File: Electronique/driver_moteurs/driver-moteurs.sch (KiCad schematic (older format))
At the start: 19 parts, among them P1 CONN_01X12, P2 CONN_01X02, P3 CONN_I2C, P4 CONN_01X04, P5 CONN_01X03, P6 CONN_SERIAL, P7 CONN_SWDIO, P8 CONN_CAN, U1 stm32f303k8t6, U2 MCP2562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

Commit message: modif moteur axe z
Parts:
- removed P1: CONN_01X12, symbol CONN_01X12
- removed P2: CONN_01X02, symbol CONN_01X02
- removed P4: CONN_01X04, symbol CONN_01X04
- removed P5: CONN_01X03, symbol CONN_01X03
- added P1: CONN_ENCODER, symbol CONN_01X04
- added P2: CONN_FREE_3, symbol CONN_01X03
- added P4: CONN_01X03, symbol CONN_01X03
- added R11: 10kR, symbol R
- added U6: MC33926, symbol MC33926
- added U7: 74HC04, symbol 74HC04
- added U8: 74LS126, symbol 74LS126
- R2: value R -> 470R
- U1: footprint (none) -> Housings_QFP:LQFP-32_7x7mm_Pitch0.8mm
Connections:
- net labels added: +9V, EN_Servo, RX_Servo, TX_Servo, TX_servo
- wire segments 94 -> 124
- no-connect marks 4 -> 0
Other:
- moved on the sheet: D1, P6, R2

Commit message: axe z routage en cours
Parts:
- removed P2: CONN_FREE_3, symbol CONN_01X03
- added P2: CONN_02_FREE, Connectors_Molex:Molex_KK-6410-02_02x2.54mm_Straight, symbol CONN_01X02
- added P5: CONN_FC, Connectors_Molex:Molex_KK-6410-02_02x2.54mm_Straight, symbol CONN_01X02
- added U10, U11, U12, U13: Trou-3, axe_z:Trou-3, symbol Trou-3
- C1, C2, C3: footprint (none) -> Capacitors_SMD:C_1206_HandSoldering
- D1: footprint (none) -> Diodes_SMD:D_SMA-SMB_Universal_Handsoldering
- JP1: footprint (none) -> Pin_Headers:Pin_Header_Straight_1x03_Pitch2.54mm
- P1, P7: footprint (none) -> Connectors_Molex:Molex_KK-6410-04_04x2.54mm_Straight
- P3, P6, P8: footprint (none) -> Connectors_Molex:Molex_KK-6410-02_02x2.54mm_Straight
- P4: value CONN_01X03 -> CONN_Servo; footprint (none) -> Connectors_Molex:Molex_KK-6410-03_03x2.54mm_Straight
- R1, R11, R2, R3: footprint (none) -> Resistors_SMD:R_1206_HandSoldering
- U2: footprint (none) -> Housings_SOIC:SOIC-8_3.9x4.9mm_Pitch1.27mm
- U6: footprint (none) -> axe_z:MC33926
- U7, U8: footprint (none) -> Housings_DIP:DIP-14_W7.62mm_Socket
- Y1: footprint (none) -> Crystals:Crystal_HC18-U_Vertical
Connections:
- net +3V3: now also P5.2 (P2)
- net GND: now also U10.1 (GND), U11.1 (GND), U12.1 (GND), U13.1 (GND)
- net at U1.26 (PB3): now also P5.1 (P1)
- net at U1.27 (PB4): now also P2.2 (P2)
- net at U1.28 (PB5): now also P2.1 (P1)

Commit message: Correction schéma driver
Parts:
- D1: symbol LED -> LED-RESCUE-driver-moteurs
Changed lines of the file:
@@
 EESchema Schematic File Version 2
+LIBS:driver-moteurs-rescue
 LIBS:power
 LIBS:device
@@
 $EndComp
 $Comp
-L LED D1
+L LED-RESCUE-driver-moteurs D1
 U 1 1 59F77A31
 P 5700 1600

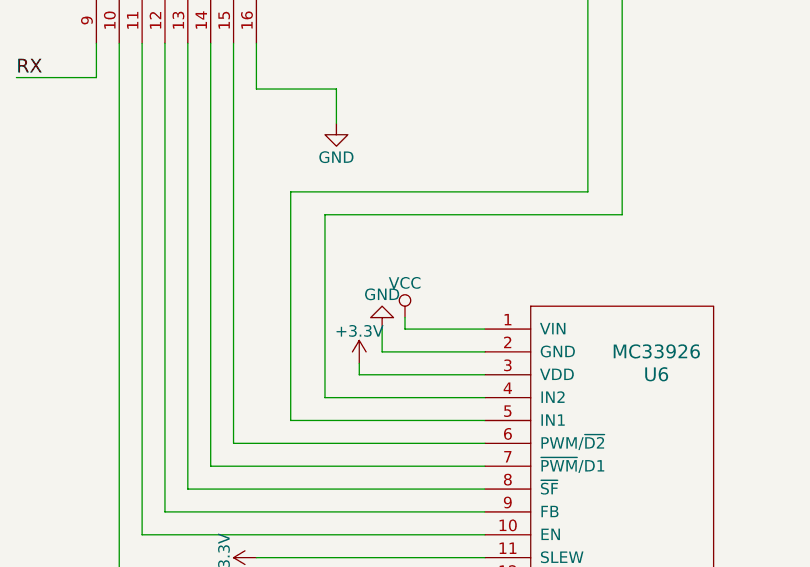
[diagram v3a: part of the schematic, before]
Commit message: Correction PCB driver moteurs
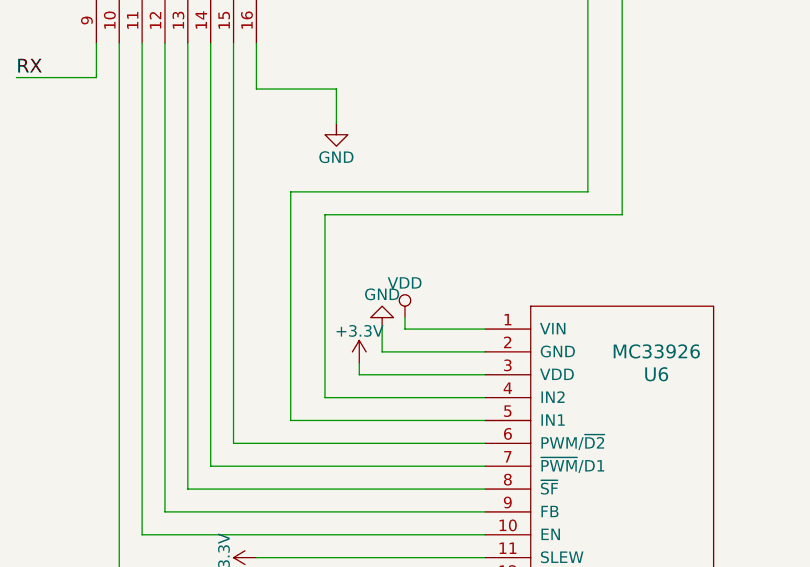
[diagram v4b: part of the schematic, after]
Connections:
- net +5V: no longer U6.1 (VIN)
- new net VDD: U6.1 (VIN)
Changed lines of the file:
@@
-	1    0    0    -1
-$EndComp
-$Comp
-L VCC #PWR016
-U 1 1 5A3E100A
-P 5900 5250
-F 0 "#PWR016" H 5900 5100 50  0001 C CNN
-F 1 "VCC" H 5900 5400 50  0000 C CNN
-F 2 "" H 5900 5250 50  0000 C CNN
-F 3 "" H 5900 5250 50  0000 C CNN
-	1    5900 5250
 	1    0    0    -1
 $EndComp
@@
 	1850 1900 1750 1900
 Connection ~ 1750 1900
+$Comp
+L VDD #PWR?
+U 1 1 5A4B0964
+P 5900 5250
+F 0 "#PWR?" H 5900 5100 50  0001 C CNN
+F 1 "VDD" H 5900 5400 50  0000 C CNN
+F 2 "" H 5900 5250 50  0001 C CNN
+F 3 "" H 5900 5250 50  0001 C CNN
+	1    5900 5250
+	1    0    0    -1
+$EndComp
 $EndSCHEMATC
